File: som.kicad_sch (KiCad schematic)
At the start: 28 parts, among them J10 Conn_FFC_Molex_5051101097, J15 Bus_DDR4_SODIMM_CUSTOM_Jetson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, M2 Jetson-Nano, T2 BSS138PW, T4 BSS138PW, T5 BSS138PW

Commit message: fix(phase1): resolve all schematic defects across som, usb, supply, csi, id-serial with zero ERC errors
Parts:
- added C103, C104: C_100n_0402, jetson-footprints:C_0402_1005Metric, symbol jetson-symbols:C_100n_0402
- SP1, SP2, SP3, SP4: now not fitted; now left out of the parts list
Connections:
- net PCIE1_TX0_N: now also C104.1; no longer J10.7
- net PCIE1_TX0_P: now also C103.1; no longer J10.6
- new net: C103.2, J10.6
- new net: C104.2, J10.7
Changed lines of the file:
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@@
 		(body_style 1)
 		(exclude_from_sim no)
-		(in_bom yes)
-		(on_board yes)
+		(in_bom no)
+		(on_board no)
 		(in_pos_files yes)
-		(dnp no)
+		(dnp yes)
 		(fields_autoplaced yes)
 		(property "Reference" "SP3"
@@
 		(body_style 1)
 		(exclude_from_sim no)
-		(in_bom yes)
-		(on_board yes)
+		(in_bom no)
+		(on_board no)
 		(in_pos_files yes)
-		(dnp no)
+		(dnp yes)
 		(property "Reference" "SP2"
 			(at 354.965 215.9 0)
@@
 		(body_style 1)
 		(exclude_from_sim no)
-		(in_bom yes)
-		(on_board yes)
+		(in_bom no)
+		(on_board no)
 		(in_pos_files yes)
-		(dnp no)
+		(dnp yes)
 		(property "Reference" "SP4"
 			(at 326.39 244.475 0)
@@
 		(body_style 1)
 		(exclude_from_sim no)
-		(in_bom yes)
-		(on_board yes)
+		(in_bom no)
+		(on_board no)
 		(in_pos_files yes)
-		(dnp no)
+		(dnp yes)
 		(property "Reference" "SP1"
 			(at 326.39 218.44 0)
@@
 	(symbol
 		(lib_id "jetson-symbols:GND")
-		(at 364.49 43.18 0)
+		(at 364.49 40.64 0)
 		(unit 1)
 		(body_style 1)
@@
 		(dnp no)
 		(property "Reference" "#GND_045"
-			(at 364.49 43.18 0)
+			(at 364.49 40.64 0)
 			(hide yes)
 			(show_name no)
@@
 		)
 		(property "Footprint" ""
-			(at 364.49 43.18 0)
+			(at 364.49 40.64 0)
 			(hide yes)
 			(show_name no)
@@
 		)
 		(property "Datasheet" ""
-			(at 364.49 43.18 0)
+			(at 364.49 40.64 0)
 			(hide yes)
 			(show_name no)
@@
 		)
 		(property "Description" ""
-			(at 364.49 43.18 0)
+			(at 364.49 40.64 0)
 			(show_name no)
 			(do_not_autoplace no)
@@
 		)
 	)
+	(symbol
+		(lib_id "jetson-symbols:C_100n_0402")
+		(at 274.32 45.72 0)
+		(unit 1)
+		(body_style 1)
+		(exclude_from_sim no)
+		(in_bom yes)
+		(on_board yes)
+		(in_pos_files yes)
+		(dnp no)
+		(fields_autoplaced yes)
+		(property "Reference" "C103"
+			(at 274.32 41.91 0)
+			(effects (font (size 1.27 1.27)) (justify left))
+		)
+		(property "Value" "C_100n_0402"
+			(at 274.32 49.53 0)
+			(effects (font (size 1.27 1.27)) (justify left))
+		)
+		(property "Footprint" "jetson-footprints:C_0402_1005Metric"
+			(at 274.32 45.72 0)
+			(hide yes)
+			(effects (font (size 1.27 1.27)))
+		)
+		(pin "1")
+		(pin "2")
+		(instances
+			(project "Jetson-AI-Cam-CopperPilot"
+				(path "/9df9f3e2-e127-4935-b743-4d95c8ce9b2e/00000000-0000-0000-0000-0000610accab"
+					(reference "C103")
+					(unit 1)
+				)
+			)
+		)
+	)
+	(symbol
+		(lib_id "jetson-symbols:C_100n_0402")
+		(at 274.32 48.26 0)
+		(unit 1)
+		(body_style 1)
+		(exclude_from_sim no)
+		(in_bom yes)
+		(on_board yes)
+		(in_pos_files yes)
+		(dnp no)
+		(fields_autoplaced yes)
+		(property "Reference" "C104"
+			(at 274.32 44.45 0)
+			(effects (font (size 1.27 1.27)) (justify left))
+		)
+		(property "Value" "C_100n_0402"
+			(at 274.32 52.07 0)
+			(effects (font (size 1.27 1.27)) (justify left))
+		)
+		(property "Footprint" "jetson-footprints:C_0402_1005Metric"
+			(at 274.32 48.26 0)
+			(hide yes)
+			(effects (font (size 1.27 1.27)))
+		)
+		(pin "1")
+		(pin "2")
+		(instances
+			(project "Jetson-AI-Cam-CopperPilot"
+				(path "/9df9f3e2-e127-4935-b743-4d95c8ce9b2e/00000000-0000-0000-0000-0000610accab"
+					(reference "C104")
+					(unit 1)
+				)
+			)
+		)
+	)
 	(label "PMIC_BBAT"
 		(at 90.17 50.8 180)
@@
 		)
 	)
-	(wire
-		(pts
-			(xy 289.56 168.91) (xy 289.56 171.45)
-		)
-		(stroke
-			(width 0)
-			(type default)
-		)
-	)
-	(wire
-		(pts
-			(xy 267.97 45.72) (xy 290.83 45.72)
-		)
-		(stroke
-			(width 0)
-			(type default)
-		)
-	)
+	(wire (pts (xy 267.97 45.72) (xy 274.32 45.72)) (stroke (width 0) (type default)))
+	(wire (pts (xy 279.4 45.72) (xy 290.83 45.72)) (stroke (width 0) (type default)))
 	(wire
 		(pts
@@
 		)
 	)
-	(wire
-		(pts
-			(xy 364.49 40.64) (xy 364.49 43.18)
-		)
-		(stroke
-			(width 0)
-			(type default)
-		)
-	)
-	(wire
-		(pts
-			(xy 267.97 48.26) (xy 290.83 48.26)
-		)
-		(stroke
-			(width 0)
-			(type default)
-		)
-	)
+	(wire (pts (xy 267.97 48.26) (xy 274.32 48.26)) (stroke (width 0) (type default)))
+	(wire (pts (xy 279.4 48.26) (xy 290.83 48.26)) (stroke (width 0) (type default)))
 	(wire
 		(pts
@@
 		)
 		(stroke
+			(width 0)
+			(type default)
+		)
+	)
+	(wire
+		(pts
+			(xy 289.56 168.91) (xy 289.56 171.45)
+		)
+		(stroke

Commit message: fix(schematic): resolve electrical omissions, CSI pairs, CAN power, DNP flags, and ERC stubs
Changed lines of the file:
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@@
-	(wire
-		(pts
-			(xy 187.96 67.31) (xy 187.96 71.12)
-		)
-		(stroke
-			(width 0)
-			(type default)
-		)
-	)
 	(wire
 		(pts
@@
 	(wire
 		(pts
-			(xy 316.23 181.61) (xy 316.23 184.15)
-		)
-		(stroke
-			(width 0)
-			(type default)
-		)
-	)
-	(wire
-		(pts
 			(xy 294.64 102.87) (xy 294.64 105.41)
 		)
@@
 		(pts
 			(xy 207.01 146.05) (xy 193.04 146.05)
-		)
-		(stroke
-			(width 0)
-			(type default)
-		)
-	)
-	(wire
-		(pts
-			(xy 316.23 166.37) (xy 316.23 168.91)
 		)
 		(stroke
@@
 	(wire
 		(pts
-			(xy 375.92 66.04) (xy 375.92 62.23)
-		)
-		(stroke
-			(width 0)
-			(type default)
-		)
-	)
-	(wire
-		(pts
 			(xy 339.09 132.08) (xy 342.9 132.08)
 		)
@@
 		)
 		(stroke
-			(width 0)
-			(type default)
-		)
-	)
-	(wire
-		(pts
-			(xy 184.15 67.31) (xy 184.15 68.58)
-		)
-		(stroke

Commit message: fix(sch): ground EEPROM WP, mark unused stubs as no-connect, and resolve all ERC warnings
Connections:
- net EGND is gone; now on net GND: SP4.1
- net #PWR_BUTTON: no longer names the net of J15.240 (SLEEP/~{WAKE})
- net ENET_LED0: no longer names the net of J15.194 (GBE_LED_ACT)
- net ENET_LED1: no longer names the net of J15.188 (GBE_LED_LINK)
- net ENET_TRD0_N: no longer names the net of J15.184 (GBE_MDI0_N)
- net ENET_TRD0_P: no longer names the net of J15.186 (GBE_MDI0_P)
- net ENET_TRD1_N: no longer names the net of J15.190 (GBE_MDI1_N)
- net ENET_TRD1_P: no longer names the net of J15.192 (GBE_MDI1_P)
- net ENET_TRD2_N: no longer names the net of J15.196 (GBE_MDI2_N)
- net ENET_TRD2_P: no longer names the net of J15.198 (GBE_MDI2_P)
- net ENET_TRD3_N: no longer names the net of J15.202 (GBE_MDI3_N)
- net ENET_TRD3_P: no longer names the net of J15.204 (GBE_MDI3_P)
- net PCIE0_CLK_N: no longer names the net of J15.160 (PCIE0_CLK_N)
- net PCIE0_CLK_P: no longer names the net of J15.162 (PCIE0_CLK_P)
- net PCIE0_RX0_N: no longer names the net of J15.131 (PCIE0_RX0_N)
- net PCIE0_RX0_P: no longer names the net of J15.133 (PCIE0_RX0_P)
- net PCIE0_RX1_N: no longer names the net of J15.137 (PCIE0_RX1_N)
- net PCIE0_RX1_P: no longer names the net of J15.139 (PCIE0_RX1_P)
- net PCIE0_RX2_N: no longer names the net of J15.149 (PCIE0_RX2_N)
- net PCIE0_RX2_P: no longer names the net of J15.151 (PCIE0_RX2_P)
- net PCIE0_RX3_N: no longer names the net of J15.155 (PCIE0_RX3_N)
- net PCIE0_RX3_P: no longer names the net of J15.157 (PCIE0_RX3_P)
- net PCIE0_TX0_N: no longer names the net of J15.134 (PCIE0_TX0_N)
- net PCIE0_TX0_P: no longer names the net of J15.136 (PCIE0_TX0_P)
- net PCIE0_TX1_N: no longer names the net of J15.140 (PCIE0_TX1_N)
- net PCIE0_TX1_P: no longer names the net of J15.142 (PCIE0_TX1_P)
- net PCIE0_TX2_N: no longer names the net of J15.148 (PCIE0_TX2_N)
- net PCIE0_TX2_P: no longer names the net of J15.150 (PCIE0_TX2_P)
- net PCIE0_TX3_N: no longer names the net of J15.154 (PCIE0_TX3_N)
- net PCIE0_TX3_P: no longer names the net of J15.156 (PCIE0_TX3_P)
- net PEX_L0_CLKREQ_N: no longer names the net of J15.180 (~{PCIE0_CLKREQ})
- net PEX_L0_RST_N: no longer names the net of J15.181 (~{PCIE0_RST})
- net VSYNC_CAM1_1: no longer names the net of J15.228 (GPIO13)
- net VSYNC_CAM1_2: no longer names the net of J15.216 (GPIO11)
- net VSYNC_CAM2_2: no longer names the net of J15.130 (GPIO06)
- net \PEWAKE_3V3: no longer names the net of J15.179 (~{PCIE_WAKE})
- no-connect marks 42 -> 77

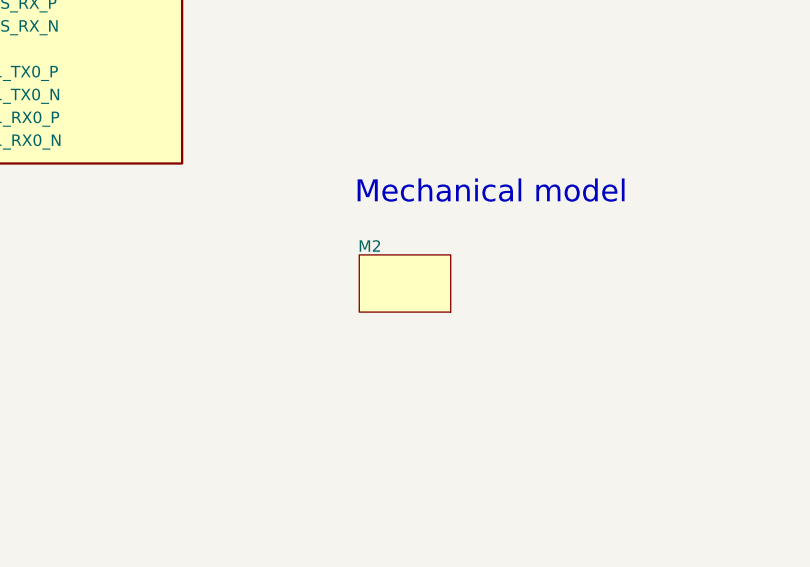
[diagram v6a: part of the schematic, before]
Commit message: feat(release): resolve all ERC/DRC/parity issues, complete 8-layer routing, and generate JLCPCB fab outputs
Resolve all schematic ERC violations, PCB DRC errors/warnings, schematic-to-PCB parity mismatches, and LCSC BOM/CPL fields, and package 8-layer Gerbers, drills, BOM, and CPL for JLCPCB manufacturing.

Co-Authored-By: CopperPilot <noreply@copperpilot.ai>
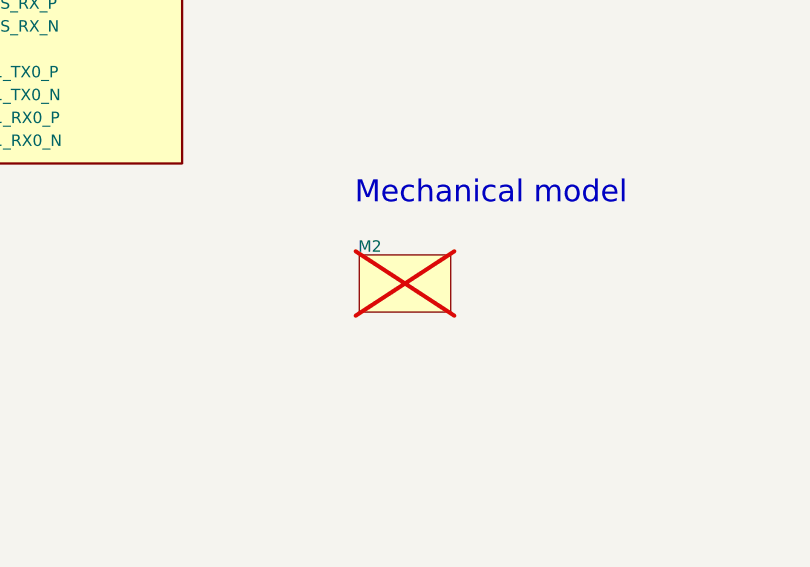
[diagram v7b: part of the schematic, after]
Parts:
- BAT1: LCSC (none) -> C86703
- BOOT1, PWR1, USER1: LCSC (none) -> C72043
- C10, C11: LCSC (none) -> C134785
- C103, C104: LCSC (none) -> C1525; MPN (none) -> GRM155R61H104KE14D
- FB2: LCSC (none) -> C145764
- J10: LCSC (none) -> C283651
- J15: LCSC (none) -> C429199
- M2: now not fitted
- R111, R14, R97: LCSC (none) -> C25117
- R112, R113: LCSC (none) -> C25741
- R139: LCSC (none) -> C25741; now left out of the parts list
- REC1, RST1, USR1: LCSC (none) -> C140844
- SP1, SP2, SP3, SP4, SP5, SP6: LCSC (none) -> C289551
- T2, T4, T5: LCSC (none) -> C84617

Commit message: fix(sch): resolve all symbol, label, and property collisions on SoM sheet (Page 4)
Flip J10 PCIe global labels outward, stagger C103/C104 and move properties out of wire bundle, shift R112 to clear USR1 value text, hide internal pin text on BSS138PW and BAT1, stagger SP1-SP6 spacer labels, align J15A/J15C/J15F labels, and preserve 100% PCB schematic parity.

Co-Authored-By: CopperPilot <noreply@copperpilot.ai>
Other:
- note removed: "Text"
- moved on the sheet: C103, C104, M2, R112, R139
